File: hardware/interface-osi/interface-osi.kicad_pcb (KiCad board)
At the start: 2 copper layers, 124.5 x 132.1 mm, 79 parts, among them J1 KBD port, J2 Key Matrix, J3 Expansion, J4 Sound, J5 ~{RESET}, U1 74LS138, U10 74HC14, U11 4066, U2 74LS04, U3 74HC240, U4 74HC240, U5 74LS373, U6 74LS373, U7 74LS193, U8 74LS193, U9 74LS390

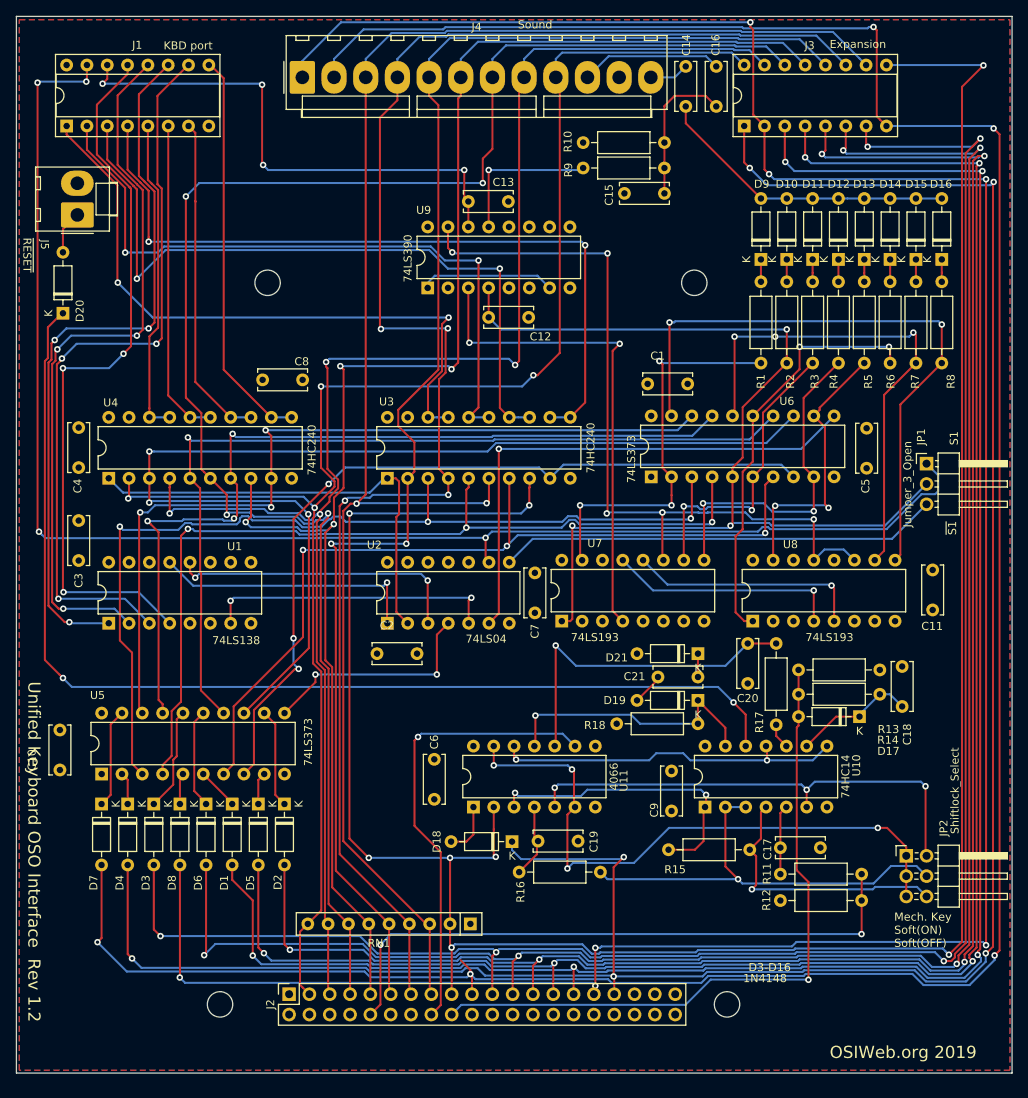
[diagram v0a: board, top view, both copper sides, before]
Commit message: Fixed multiple problems with OSI interface
- off-by-one connections to keyboard connector
- wrong demultiplexing of select signals
- 2OE on 74LS240 was not inverted, resulting in wrong circuit.
- use pre-jumpered row diodes.
- fixed off-grid errors on schematic
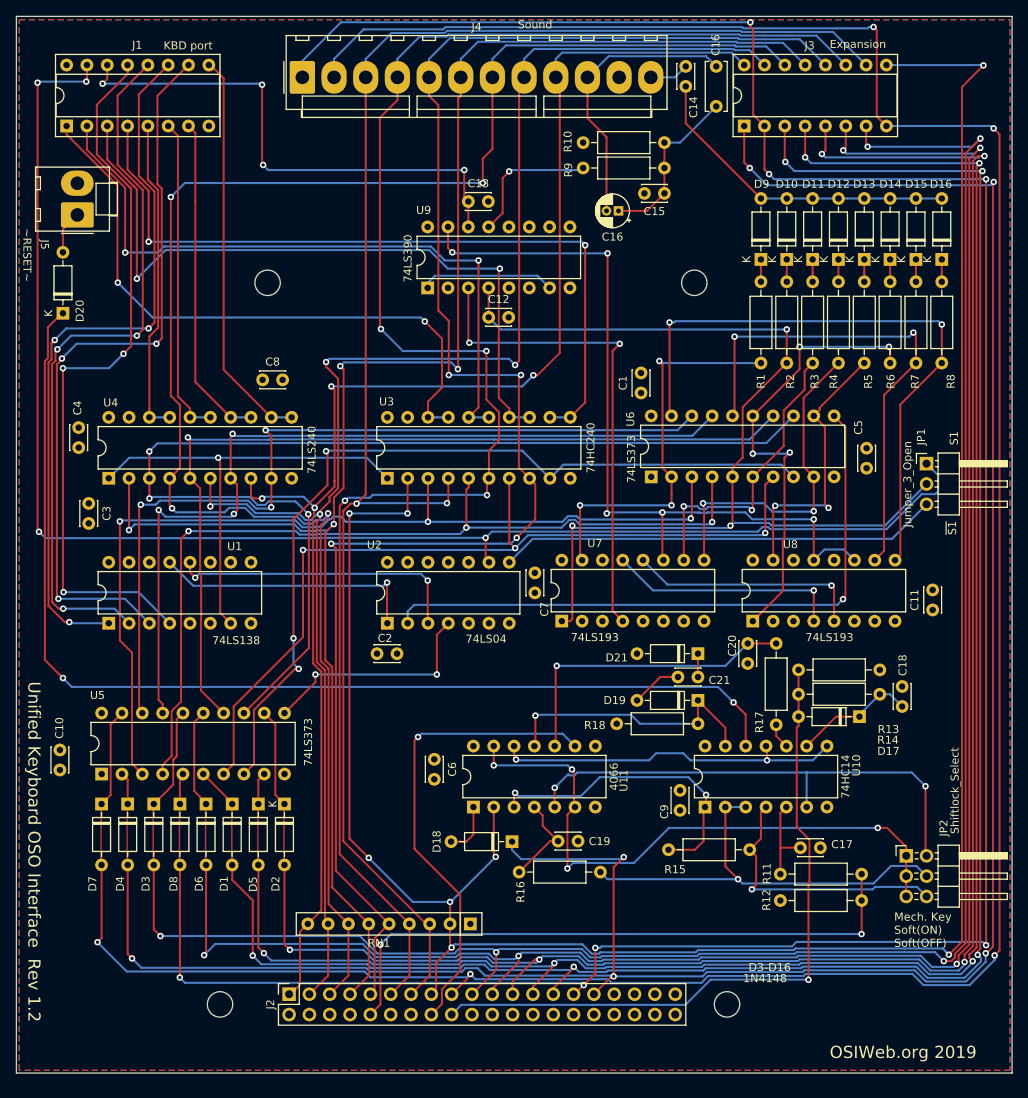
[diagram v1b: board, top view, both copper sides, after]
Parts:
- added C16: 33 uF, Capacitor_THT:CP_Radial_D4.0mm_P1.50mm, F.Cu at (226.4, 75.1)
- C1, C10, C11, C12, C13, C14, C17, C18, C19, C2, C20, C21, C3, C4, C5, C6, C7, C8, C9: footprint Capacitor_THT:C_Disc_D6.0mm_W2.5mm_P5.00mm -> Capacitor_THT:C_Disc_D3.0mm_W2.0mm_P2.50mm
- C15: value C -> 0.1uF; footprint Capacitor_THT:C_Disc_D6.0mm_W2.5mm_P5.00mm -> Capacitor_THT:C_Disc_D3.0mm_W2.0mm_P2.50mm
- D1, D2, D3, D4, D5, D6, D7, D8: footprint Diode_THT:D_DO-35_SOD27_P7.62mm_Horizontal -> unikbd:D_DO-35_SOD27_P7.62mm_Horizontal_bypassed
- J5: value ~{RESET} -> ~RESET~
- R10: value R_US -> 1k
- R9: value R_US -> 4.7k
- U4: value 74HC240 -> 74LS240
- moved C9 2.64 mm to (234.1, 147.5)
- moved C3 2.48 mm to (160.2, 111.7)
- moved C1 1.40 mm to (229.2, 97.9), turned to 90 degrees
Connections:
- J2 pad 1: Net-(J2-Pad1) -> /Col7
- J2 pad 11: /Col3 -> /Col2
- J2 pad 13: /Col2 -> /Col1
- J2 pad 15: /Col1 -> /Col0
- J2 pad 17: /Col0 -> /Row7
- J2 pad 19: /Row7 -> /Row6
- J2 pad 2: Net-(J2-Pad2) -> unconnected-(J2-Pin_2-Pad2)
- J2 pad 21: /Row6 -> /Row5
- J2 pad 22: Net-(J2-Pad22) -> unconnected-(J2-Pin_22-Pad22)
- J2 pad 23: /Row5 -> /Row4
- J2 pad 24: Net-(J2-Pad24) -> unconnected-(J2-Pin_24-Pad24)
- J2 pad 25: /Row4 -> /Row3
- J2 pad 26: Net-(J2-Pad26) -> unconnected-(J2-Pin_26-Pad26)
- J2 pad 27: /Row3 -> /Row2
- J2 pad 28: Net-(J2-Pad28) -> unconnected-(J2-Pin_28-Pad28)
- J2 pad 29: /Row2 -> /Row1
- J2 pad 3: /Col7 -> /Col6
- J2 pad 30: Net-(J2-Pad30) -> unconnected-(J2-Pin_30-Pad30)
- J2 pad 31: /Row1 -> /Row0
- J2 pad 32: Net-(J2-Pad32) -> unconnected-(J2-Pin_32-Pad32)
- J2 pad 33: /Row0 -> unconnected-(J2-Pin_33-Pad33)
- J2 pad 34: Net-(J2-Pad34) -> unconnected-(J2-Pin_34-Pad34)
- J2 pad 35: Net-(J2-Pad35) -> unconnected-(J2-Pin_35-Pad35)
- J2 pad 36: Net-(J2-Pad36) -> unconnected-(J2-Pin_36-Pad36)
- J2 pad 37: Net-(J2-Pad37) -> unconnected-(J2-Pin_37-Pad37)
- J2 pad 38: Net-(J2-Pad38) -> unconnected-(J2-Pin_38-Pad38)
- J2 pad 39: Net-(J2-Pad39) -> unconnected-(J2-Pin_39-Pad39)
- J2 pad 4: Net-(J2-Pad4) -> unconnected-(J2-Pin_4-Pad4)
- J2 pad 40: Net-(J2-Pad40) -> unconnected-(J2-Pin_40-Pad40)
- J2 pad 5: /Col6 -> /Col5
- J2 pad 6: Net-(J2-Pad6) -> unconnected-(J2-Pin_6-Pad6)
- J2 pad 7: /Col5 -> /Col4
- J2 pad 8: Net-(J2-Pad8) -> unconnected-(J2-Pin_8-Pad8)
- J2 pad 9: /Col4 -> /Col3
- U1 pad 10: Net-(U1-Pad10) -> unconnected-(U1-O5-Pad10)
- U1 pad 11: Net-(U1-Pad11) -> unconnected-(U1-O4-Pad11)
- U1 pad 14: Net-(U1-Pad14) -> unconnected-(U1-O1-Pad14)
- U1 pad 15: Net-(U1-Pad15) -> unconnected-(U1-O0-Pad15)
- U1 pad 7: Net-(U1-Pad7) -> Net-(U1-O7)
- U1 pad 9: Net-(U1-Pad9) -> unconnected-(U1-O6-Pad9)
- U2 pad 10: (no net) -> unconnected-(U2-Pad10)
- U2 pad 11: (no net) -> unconnected-(U2-Pad11)
- U2 pad 12: (no net) -> unconnected-(U2-Pad12)
- U2 pad 13: (no net) -> unconnected-(U2-Pad13)
- U2 pad 14: (no net) -> +5V
- U2 pad 2: Net-(U2-Pad2) -> /Sound/SOUND_EN
- U2 pad 5: Net-(U1-Pad7) -> unconnected-(U2-Pad5)
- U2 pad 6: /Sound/SOUND_EN -> unconnected-(U2-Pad6)
- U2 pad 7: (no net) -> GND
- U3 pad 1: Net-(U2-Pad2) -> Net-(U1-O7)
- U3 pad 2: /Col3 -> /Col0
- U3 pad 4: /Col2 -> /Col1
- U3 pad 6: /Col1 -> /Col2
- U3 pad 8: /Col0 -> /Col3
- U4 pad 1: Net-(U2-Pad2) -> Net-(U1-O7)
- U4 pad 2: /Col7 -> /Col4
- U4 pad 4: /Col6 -> /Col5
- U4 pad 6: /Col5 -> /Col6
- U4 pad 8: /Col4 -> /Col7
- U7 pad 2: Net-(U7-Pad2) -> unconnected-(U7-QB-Pad2)
- U7 pad 3: Net-(U7-Pad3) -> unconnected-(U7-QA-Pad3)
- U7 pad 6: Net-(U7-Pad6) -> unconnected-(U7-QC-Pad6)
- U7 pad 7: Net-(U7-Pad7) -> unconnected-(U7-QD-Pad7)
- U8 pad 12: Net-(U8-Pad12) -> unconnected-(U8-~{CO}-Pad12)
- U8 pad 2: Net-(U8-Pad2) -> unconnected-(U8-QB-Pad2)
- U8 pad 3: Net-(U8-Pad3) -> unconnected-(U8-QA-Pad3)
- U8 pad 6: Net-(U8-Pad6) -> unconnected-(U8-QC-Pad6)
- U8 pad 7: Net-(U8-Pad7) -> unconnected-(U8-QD-Pad7)
- U9 pad 10: Net-(U9-Pad10) -> unconnected-(U9B-Q2-Pad10)
- U9 pad 11: Net-(U9-Pad11) -> unconnected-(U9B-Q1-Pad11)
- U9 pad 5: Net-(U9-Pad5) -> unconnected-(U9A-Q1-Pad5)
- U9 pad 6: Net-(U9-Pad6) -> unconnected-(U9A-Q2-Pad6)
- U9 pad 9: Net-(U9-Pad9) -> unconnected-(U9B-Q3-Pad9)
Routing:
- net Net-(U1-O7): track 0.00 -> 58.3 mm, vias 0 -> 1
- net Net-(U2-Pad2): track 56.4 -> 0.00 mm
- net Net-(U1-Pad7): track 36.4 -> 0.00 mm, vias 2 -> 0
- net /Col3: track 185.2 -> 207.5 mm, vias 2 -> 4
- net /Sound/Noise2: track 17.7 -> 35.4 mm
- net /Col4: track 198.0 -> 215.2 mm
- net /Col7: track 199.4 -> 182.4 mm
- net /Col0: track 298.2 -> 283.3 mm
- net /Sound/SOUND_EN: track 65.9 -> 80.1 mm
- net /Col2: track 202.7 -> 211.9 mm
- net /Col5: track 210.0 -> 218.3 mm
- net /Col6: track 200.0 -> 195.0 mm
- net /Sound/KD3: track 102.3 -> 106.8 mm
- net /Sound/S5: track 52.4 -> 56.7 mm, vias 2 -> 4
- net /Col1: track 208.6 -> 204.5 mm
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
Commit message: Update version and some text strings
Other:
- board text added: "${TITLE} Rev ${REVISION}"
- board text added: "OSIWeb.org 2023"
- board text added: "OSIWeb.org 2023£"
- board text removed: "OSIWeb.org 2019"
- board text removed: "Unified Keyboard OSI Interface Rev 1.2"
- board text removed: "Unified Keyboard OSO Interface Rev 1.2"
